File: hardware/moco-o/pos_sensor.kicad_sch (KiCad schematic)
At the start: 6 parts, among them U7 AS5047x

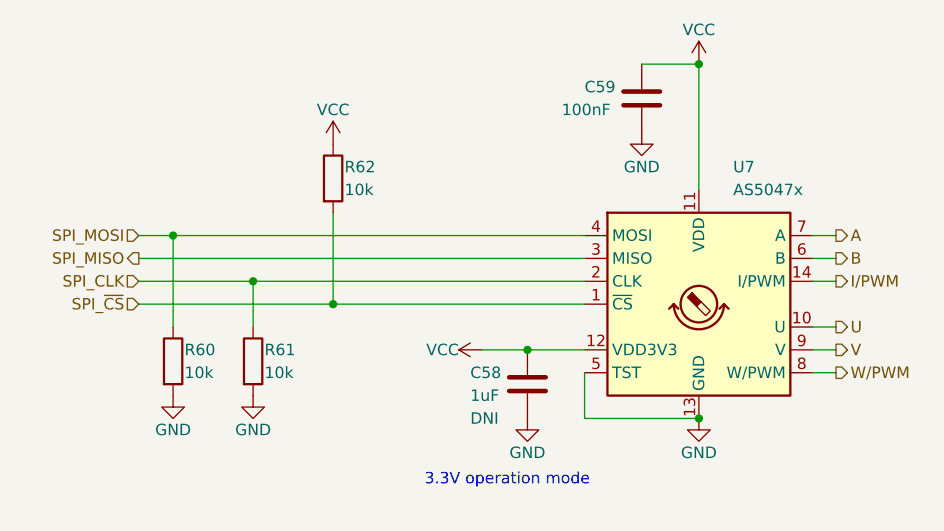
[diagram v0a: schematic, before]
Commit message: Change to DRV8323H
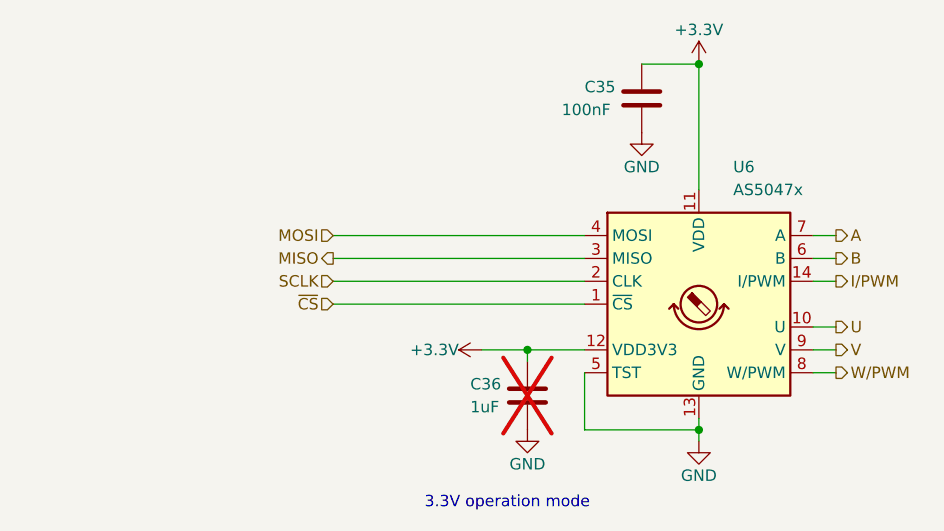
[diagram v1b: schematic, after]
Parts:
- removed R60, R61, R62: 10k, Resistor_SMD:R_0402_1005Metric, symbol Device:R
- C35: renamed from C59; footprint Capacitor_SMD:C_0402_1005Metric -> Capacitor_SMD:C_0603_1608Metric_Pad1.08x0.95mm_HandSolder
- C36: renamed from C58; footprint Capacitor_SMD:C_0402_1005Metric -> Capacitor_SMD:C_0603_1608Metric_Pad1.08x0.95mm_HandSolder; Note DNI -> (none); now not fitted
- renumbered U7 to U6
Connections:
- net SPI_CLK renamed SCLK
- net SPI_MISO renamed MISO
- net SPI_MOSI renamed MOSI
- net SPI_~{CS} renamed ~{CS}
- net VCC renamed +3.3V
